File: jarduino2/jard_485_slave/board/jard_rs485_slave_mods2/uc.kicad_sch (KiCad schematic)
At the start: 14 parts, among them J1 POWER

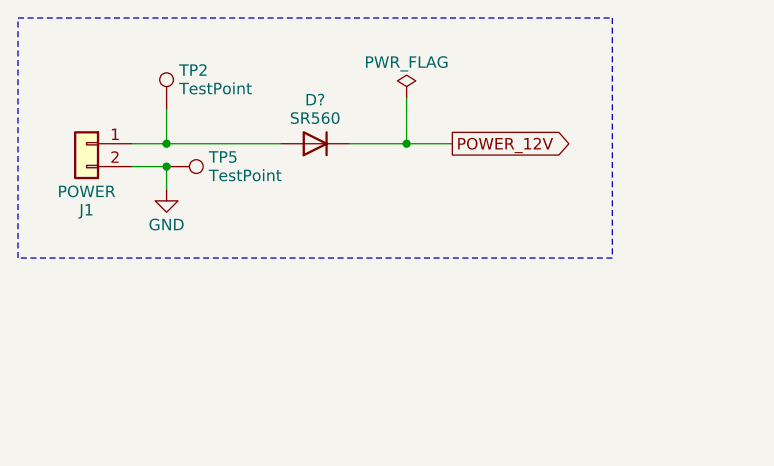
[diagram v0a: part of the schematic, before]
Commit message: Suppression du module RS485 et remplacement par le CI MAX485E lui-même. Preparation version G...
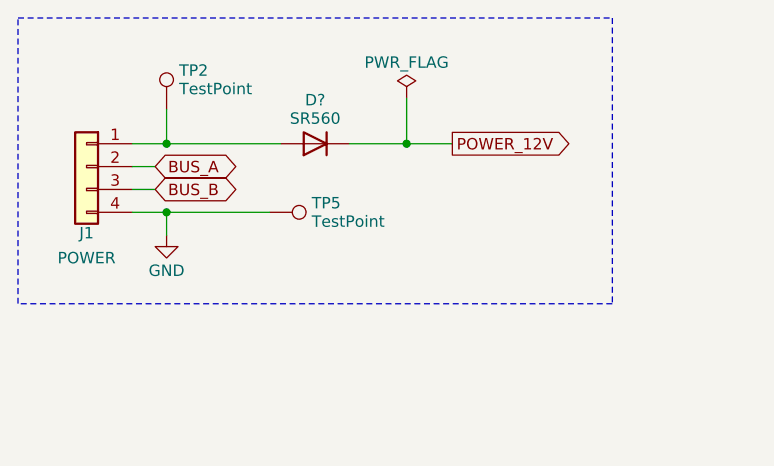
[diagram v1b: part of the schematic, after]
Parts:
- J1: footprint TerminalBlock_Phoenix:TerminalBlock_Phoenix_MKDS-1,5-2-5.08_1x02_P5.08mm_Horizontal -> TerminalBlock_Phoenix:TerminalBlock_Phoenix_MKDS-1,5-4-5.08_1x04_P5.08mm_Horizontal; symbol Connector_Generic:Conn_01x02 -> Connector_Generic:Conn_01x04
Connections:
- net GND: now also J1.4 (Pin_4); no longer J1.2 (Pin_2)
- new net BUS_A: J1.2 (Pin_2)
- new net BUS_B: J1.3 (Pin_3)
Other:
- moved on the sheet: TP5
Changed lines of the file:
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@@
   (title_block
     (title "Carte de commande d'un OYA - Esclave RS485")
-    (date "2024-05-04")
-    (rev "F0")
+    (date "2024-05-05")
+    (rev "G0")
     (company "BPC")
-    (comment 1 "Technologie avec modules Arduino / Petite carte")
+    (comment 1 "Technologie avec modules Arduino Nano / Petite carte")
     (comment 2 "Monitoring de tension d'alimentation")
     (comment 3 "1 sortie 12V/5A - 2 entrées TOR - 1 débimètre - 1 LED - Temp - RS485")
@@
   (junction (at 241.3 96.52) (diameter 0) (color 0 0 0 0)
   )
-  (junction (at 41.91 41.91) (diameter 0) (color 0 0 0 0)
+  (junction (at 41.91 46.99) (diameter 0) (color 0 0 0 0)
   )
   (no_connect (at 176.53 99.06))
@@
   (no_connect (at 176.53 81.28))
   (no_connect (at 151.13 78.74))
-  (wire (pts (xy 41.91 41.91) (xy 38.1 41.91))
+  (wire (pts (xy 41.91 46.99) (xy 38.1 46.99))
     (stroke (width 0) (type default))
   )
@@
     (stroke (width 0) (type default))
   )
+  (wire (pts (xy 38.1 44.45) (xy 40.64 44.45))
+    (stroke (width 0) (type default))
+  )
+  (wire (pts (xy 38.1 41.91) (xy 40.64 41.91))
+    (stroke (width 0) (type default))
+  )
   (wire (pts (xy 62.23 143.51) (xy 67.31 143.51))
     (stroke (width 0) (type default))
@@
     (stroke (width 0) (type default))
   )
+  (wire (pts (xy 53.34 46.99) (xy 41.91 46.99))
+    (stroke (width 0) (type default))
+  )
   (wire (pts (xy 234.95 49.53) (xy 234.95 54.61))
     (stroke (width 0) (type default))
@@
     (stroke (width 0) (type default))
   )
-  (wire (pts (xy 41.91 44.45) (xy 41.91 41.91))
+  (wire (pts (xy 41.91 49.53) (xy 41.91 46.99))
     (stroke (width 0) (type default))
   )
@@
     (fill (type none))
   )
-  (rectangle (start 25.4 25.4) (end 91.44 52.07)
+  (rectangle (start 25.4 25.4) (end 91.44 57.15)
     (stroke (width 0) (type dash))
     (fill (type none))
@@
     )
   )
+  (global_label "BUS_A" (shape tri_state) (at 40.64 41.91 0) (fields_autoplaced)
+    (effects (font (size 1.27 1.27)) (justify left))
+    (property "Intersheetrefs" "${INTERSHEET_REFS}" (at 50.5233 41.91 0)
+      (effects (font (size 1.27 1.27)) (justify left) hide)
+    )
+  )
   (global_label "A3" (shape output) (at 264.16 151.13 0) (fields_autoplaced)
     (effects (font (size 1.27 1.27)) (justify left))
@@
     (effects (font (size 1.27 1.27)) (justify left))
     (property "Intersheetrefs" "${INTERSHEET_REFS}" (at 184.2739 88.9 0)
+      (effects (font (size 1.27 1.27)) (justify left) hide)
+    )
+  )
+  (global_label "BUS_B" (shape tri_state) (at 40.64 44.45 0) (fields_autoplaced)
+    (effects (font (size 1.27 1.27)) (justify left))
+    (property "Intersheetrefs" "${INTERSHEET_REFS}" (at 50.7047 44.45 0)
       (effects (font (size 1.27 1.27)) (justify left) hide)
     )
@@
     )
   )
-  (symbol (lib_id "Connector:TestPoint") (at 41.91 41.91 270) (unit 1)
-    (in_bom yes) (on_board yes) (dnp no) (fields_autoplaced)
-    (property "Reference" "TP5" (at 46.609 40.886 90)
+  (symbol (lib_id "Connector:TestPoint") (at 53.34 46.99 270) (unit 1)
+    (in_bom yes) (on_board yes) (dnp no) (fields_autoplaced)
+    (property "Reference" "TP5" (at 58.039 45.966 90)
       (effects (font (size 1.27 1.27)) (justify left))
     )
-    (property "Value" "TestPoint" (at 46.609 42.934 90)
+    (property "Value" "TestPoint" (at 58.039 48.014 90)
       (effects (font (size 1.27 1.27)) (justify left))
     )
-    (property "Footprint" "TestPoint:TestPoint_Pad_D1.5mm" (at 41.91 46.99 0)
-      (effects (font (size 1.27 1.27)) hide)
-    )
-    (property "Datasheet" "~" (at 41.91 46.99 0)
-      (effects (font (size 1.27 1.27)) hide)
-    )
-    (property "RefFabricant" "" (at 41.91 41.91 0)
-      (effects (font (size 1.27 1.27)) hide)
-    )
-    (property "RefFournisseur" "" (at 41.91 41.91 0)
-      (effects (font (size 1.27 1.27)) hide)
-    )
-    (property "Price" "0" (at 41.91 41.91 0)
+    (property "Footprint" "TestPoint:TestPoint_Pad_D1.5mm" (at 53.34 52.07 0)
+      (effects (font (size 1.27 1.27)) hide)
+    )
+    (property "Datasheet" "~" (at 53.34 52.07 0)
+      (effects (font (size 1.27 1.27)) hide)
+    )
+    (property "RefFabricant" "" (at 53.34 46.99 0)
+      (effects (font (size 1.27 1.27)) hide)
+    )
+    (property "RefFournisseur" "" (at 53.34 46.99 0)
+      (effects (font (size 1.27 1.27)) hide)
+    )
+    (property "Price" "0" (at 53.34 46.99 0)
       (effects (font (size 1.27 1.27)) hide)
     )
@@
     )
   )
-  (symbol (lib_id "power:GND") (at 41.91 44.45 0) (unit 1)
-    (in_bom yes) (on_board yes) (dnp no) (fields_autoplaced)
-    (property "Reference" "#PWR?" (at 41.91 50.8 0)
-      (effects (font (size 1.27 1.27)) hide)
-    )
-    (property "Value" "GND" (at 41.91 48.395 0)
-      (effects (font (size 1.27 1.27)))
-    )
-    (property "Footprint" "" (at 41.91 44.45 0)
-      (effects (font (size 1.27 1.27)) hide)
-    )
-    (property "Datasheet" "" (at 41.91 44.45 0)
+  (symbol (lib_id "power:GND") (at 41.91 49.53 0) (unit 1)
+    (in_bom yes) (on_board yes) (dnp no) (fields_autoplaced)
+    (property "Reference" "#PWR?" (at 41.91 55.88 0)
+      (effects (font (size 1.27 1.27)) hide)
+    )
+    (property "Value" "GND" (at 41.91 53.475 0)
+      (effects (font (size 1.27 1.27)))
+    )
+    (property "Footprint" "" (at 41.91 49.53 0)
+      (effects (font (size 1.27 1.27)) hide)
+    )
+    (property "Datasheet" "" (at 41.91 49.53 0)
       (effects (font (size 1.27 1.27)) hide)
     )
@@
     )
   )
-  (symbol (lib_id "Connector_Generic:Conn_01x02") (at 33.02 39.37 0) (mirror y) (unit 1)
+  (symbol (lib_id "Connector_Generic:Conn_01x04") (at 33.02 41.91 0) (mirror y) (unit 1)
     (in_bom yes) (on_board yes) (dnp no)
-    (property "Reference" "J1" (at 33.02 46.76 0)
-      (effects (font (size 1.27 1.27)))
-    )
-    (property "Value" "POWER" (at 33.02 44.712 0)
-      (effects (font (size 1.27 1.27)))
-    )
-    (property "Footprint" "TerminalBlock_Phoenix:TerminalBlock_Phoenix_MKDS-1,5-2-5.08_1x02_P5.08mm_Horizontal" (at 33.02 39.37 0)
-      (effects (font (size 1.27 1.27)) hide)
-    )
-    (property "Datasheet" "~" (at 33.02 39.37 0)
-      (effects (font (size 1.27 1.27)) hide)
-    )
-    (property "Description" "Bornier 2 contacts 5.08mm" (at 33.02 39.37 0)
-      (effects (font (size 1.27 1.27)) hide)
-    )
-    (property "Fabricant" "PHOENIX CONTACT" (at 33.02 39.37 0)
-      (effects (font (size 1.27 1.27)) hide)
-    )
-    (property "Fournisseur" "Farnell" (at 33.02 39.37 0)
+    (property "Reference" "J1" (at 33.02 49.3 0)
+      (effects (font (size 1.27 1.27)))
+    )
+    (property "Value" "POWER" (at 33.02 52.07 0)
+      (effects (font (size 1.27 1.27)))
+    )
+    (property "Footprint" "TerminalBlock_Phoenix:TerminalBlock_Phoenix_MKDS-1,5-4-5.08_1x04_P5.08mm_Horizontal" (at 33.02 41.91 0)
+      (effects (font (size 1.27 1.27)) hide)
+    )
+    (property "Datasheet" "~" (at 33.02 41.91 0)
+      (effects (font (size 1.27 1.27)) hide)
+    )
+    (property "Description" "Bornier 2 contacts 5.08mm" (at 33.02 41.91 0)
+      (effects (font (size 1.27 1.27)) hide)
+    )
+    (property "Fabricant" "PHOENIX CONTACT" (at 33.02 41.91 0)
+      (effects (font (size 1.27 1.27)) hide)
+    )
+    (property "Fournisseur" "Farnell" (at 33.02 41.91 0)
       (effects (font (size 1.27 1.27)) hide)
     )
     (pin "1")
     (pin "2")
-    (instances
-      (project "jard_rs485_slave_mods2"
+    (pin "3")
+    (pin "4")
+    (instances
+      (project "jard_rs485_slave_mods2"

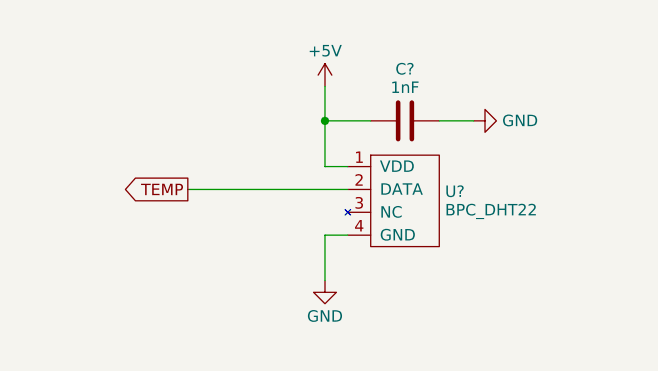
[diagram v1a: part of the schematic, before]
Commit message: Amélioration découplage RS485, MOS sur autre face
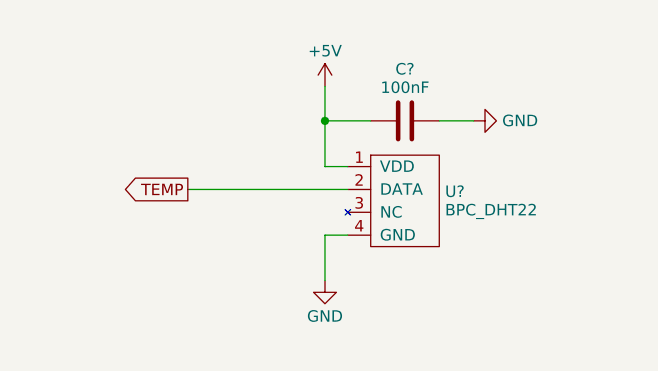
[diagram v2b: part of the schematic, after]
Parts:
- C?: value 1nF -> 100nF
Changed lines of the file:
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@@
     (rev "G0")
     (company "BPC")
-    (comment 1 "Technologie avec modules Arduino Nano / Petite carte")
+    (comment 1 "Technologie avec module Arduino Nano / Petite carte")
     (comment 2 "Monitoring de tension d'alimentation")
     (comment 3 "1 sortie 12V/5A - 2 entrées TOR - 1 débimètre - 1 LED - Temp - RS485")
@@
       (effects (font (size 1.27 1.27)))
     )
-    (property "Value" "1nF" (at 243.84 33.139 90)
+    (property "Value" "100nF" (at 243.84 33.139 90)
       (effects (font (size 1.27 1.27)))
     )
